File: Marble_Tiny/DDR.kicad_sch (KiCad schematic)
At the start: 53 parts, among them U2 AS4C256M16D3

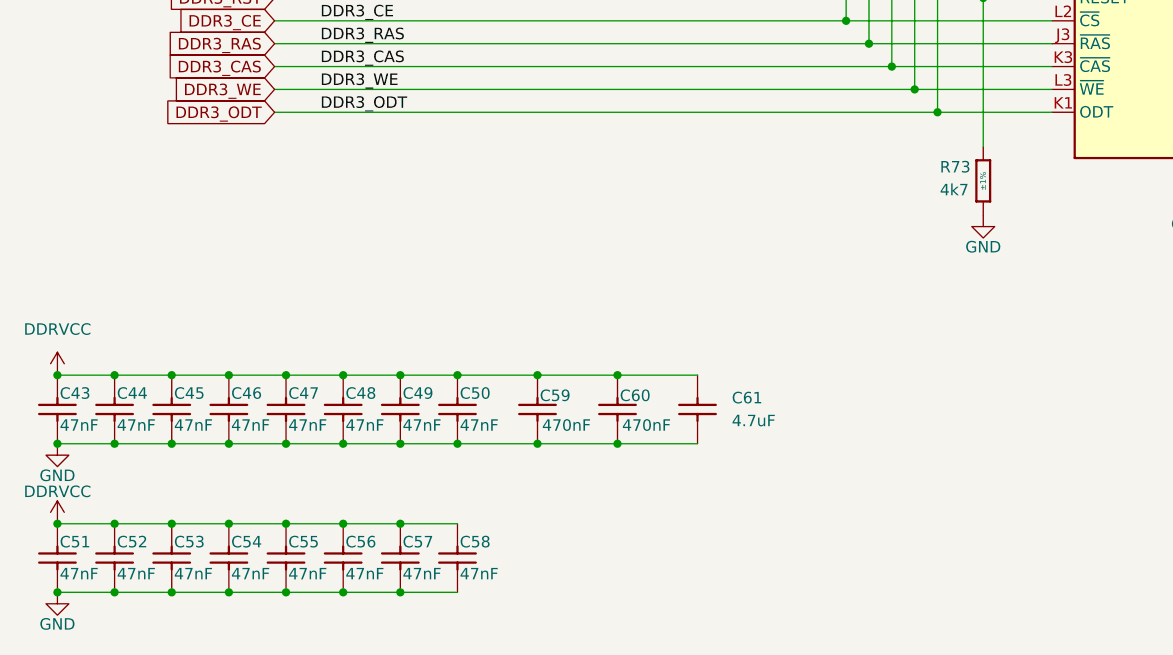
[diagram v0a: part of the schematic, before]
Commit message: components placement done, fixed issue with PCB
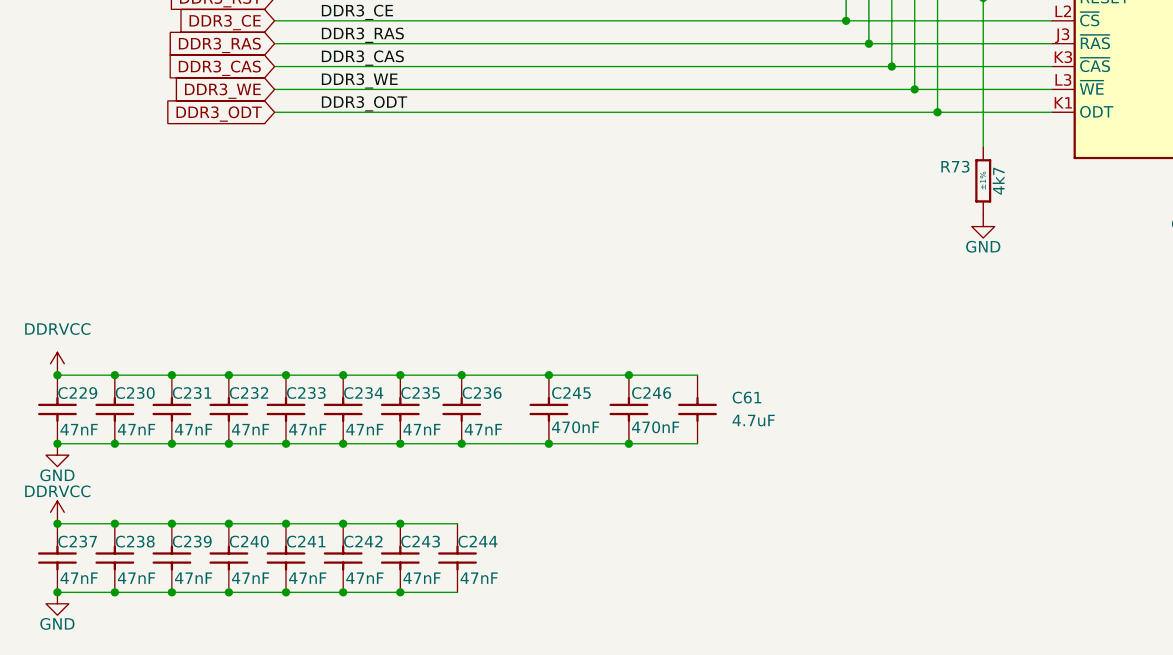
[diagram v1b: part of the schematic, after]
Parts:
- removed C43, C44, C45, C46, C47, C48, C49, C50, C51, C52, C53, C54, C55, C56, C57, C58: CC0402_47NF_25V_10%_X7R, Capacitors SMD:CAPC1005X55N, symbol Capacitors SMD:CC0402_47NF_25V_10%_X7R
- removed C59, C60: CC0402_470NF_50V_10%_X5R, Capacitors SMD:CAPC1005X55N, symbol Capacitors SMD:CC0402_470NF_50V_10%_X5R
- added C229, C230, C231, C232, C233, C234, C235, C236, C237, C238, C239, C240, C241, C242, C243, C244: CC0201_47NF_6.3V_10%_X5R, Capacitors SMD:CAPC0603X33N, symbol Capacitors SMD:CC0201_47NF_6.3V_10%_X5R
- added C245, C246: CC0201_470NF_4V_20%_X5R, Capacitors SMD:CAPC0603X33N, symbol Capacitors SMD:CC0201_470NF_4V_20%_X5R
- R73: value R1210_4K7_1%_0.5W_100PPM -> R0402_4K7_1%_0.0625W_100PPM; footprint Resistors SMD:RESC3225X70N -> Resistors SMD:RESC1005X40N; symbol Resistors SMD:R1210_4K7_1%_0.5W_100PPM -> Resistors SMD:R0402_4K7_1%_0.0625W_100PPM; Author CERN DEM WB -> CERN DEM JLC; Case 1210 -> 0402; ComponentHeight 0.7mm -> (none); CreateDate 06/30/21 00:00:00 -> 12/03/07 00:00:00; Footprint Ref RESC3225X70N -> RESC1005X40N; HelpURL \\cern.ch\dfs\Applications\Altium\Datasheets\R1210_VISHAY_C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 -> \\cern.ch\dfs\Applications\Altium\Datasheets\R0402_Phycomp_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; LatestRevisionDate 06/30/21 00:00:00 -> 10/17/12 00:00:00; Manufacturer Part Number R1210_4K7_1%_0.5W_100PPM -> R0402_4K7_1%_0.0625W_100PPM; Manufacturer1 ComponentHeight 0.7mm -> 0.4mm; Manufacturer1 Example VISHAY -> YAGEO PHYCOMP; Manufacturer1 Part Number CRCW12104K70FK -> 232270674702L; Part Number R1210_4K7_1%_0.5W_100PPM -> R0402_4K7_1%_0.0625W_100PPM; Power 0.5W -> 0.0625W; Status None -> Not Recommended
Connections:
- net DDRVCC: now also C229.2, C230.2, C231.2, C232.2, C233.2, C234.2, C235.2, C236.2, C237.2, C238.2, C239.2, C240.2, C241.2, C242.2, C243.2, C244.2, C245.2, C246.2
- net GND: now also C229.1, C230.1, C231.1, C232.1, C233.1, C234.1, C235.1, C236.1, C237.1, C238.1, C239.1, C240.1, C241.1, C242.1, C243.1, C244.1, C245.1, C246.1
